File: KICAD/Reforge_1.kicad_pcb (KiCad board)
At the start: 2 copper layers, 61 x 77.8 mm, 92 parts, among them J1 USB_C_Receptacle_USB2.0_16P, J10 Conn_01x14_Pin, J11 Conn_01x12_Pin, J12 Conn_01x12_Pin, J14 Conn_01x12_Pin, J15 Conn_01x12_Pin, J3 Conn_01x02, J8 Conn_01x12_Pin, J9 Conn_01x14_Pin, Q1 SS8050, Q2 SS8050, SW1 SW_Push, SW2 SW_Push, U11 SN74LVC2G125DCUR, U2 CP2102N-Axx-xQFN28, U3 ICE40UP5K-SG48ITR, U4 AP2112K-1.2, U5 ESP32-WROOM-32D, U6 AMS1117-3.3, U8 W25Q32JVSS, Y1 SG-210STF

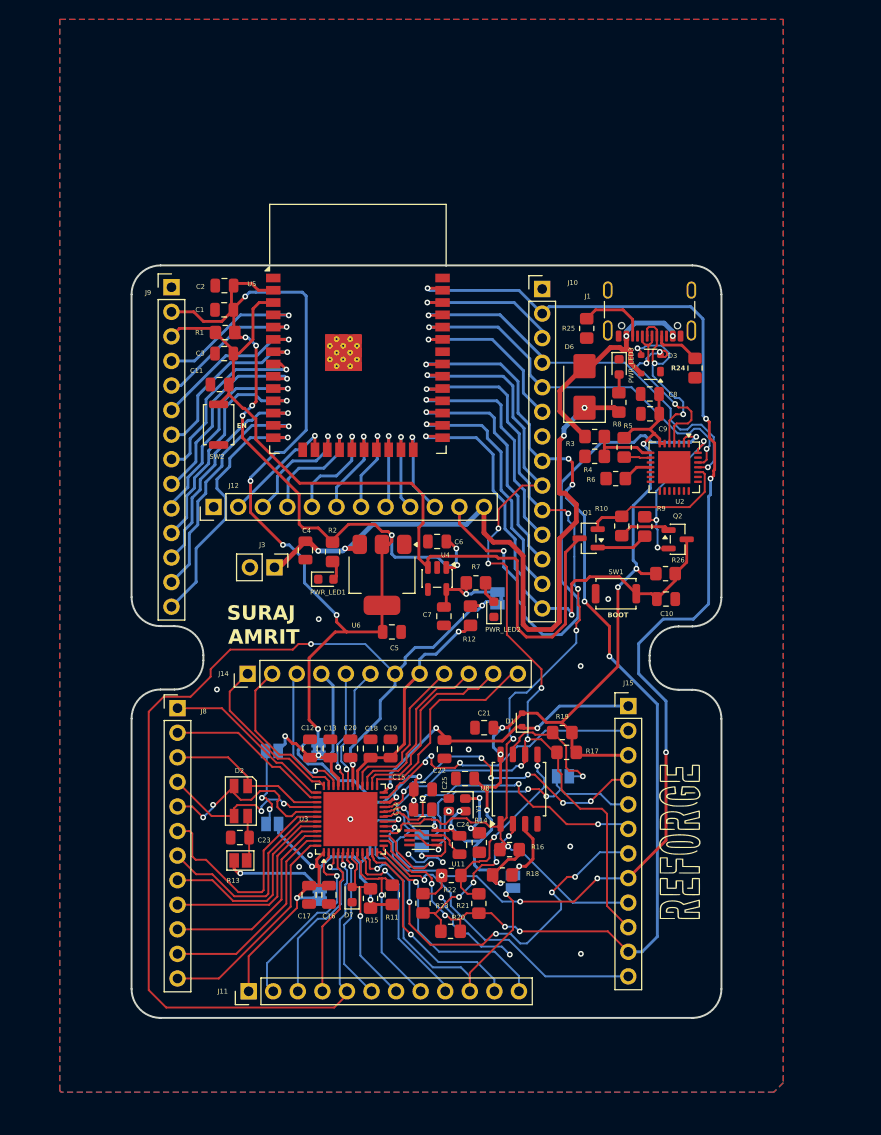
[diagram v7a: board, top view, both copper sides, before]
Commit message: Updated Schematic, Added mounting hole and some updates in PCB
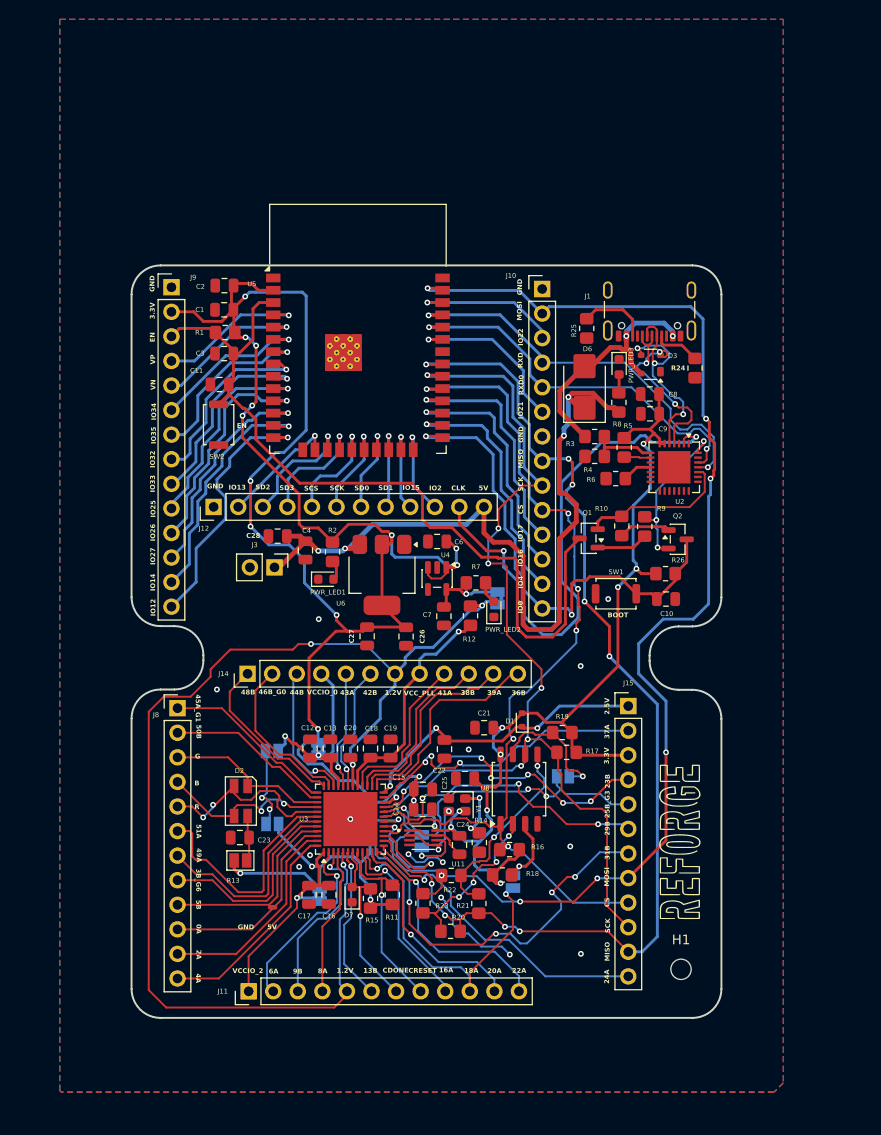
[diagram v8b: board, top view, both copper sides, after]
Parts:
- removed C5: 10uF, Capacitor_SMD:C_0805_2012Metric
- added C26: 22uF, Capacitor_SMD:C_0805_2012Metric, F.Cu at (136.7, 85.5)
- added C27: 0.1uF, Capacitor_SMD:C_0805_2012Metric, F.Cu at (132.7, 85.5)
- added C28: 0.1uF, Capacitor_SMD:C_0805_2012Metric, F.Cu at (123.4, 75.1)
- added H1: MountingHole, MountingHole:MountingHole_2.1mm, F.Cu at (165.1, 119.9)
- C4: value 22uF -> 10uF
- R10, R9: value 10R(5%) -> 10k(5%)
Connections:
- U4 pad 3: /EN -> /VDD33
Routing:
- net /VDD33: track 308.7 -> 316.5 mm
- net /EXT_5V: track 74.6 -> 81.7 mm
- net /EN: track 88.6 -> 84.2 mm
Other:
- board text added: "0A"
- board text added: "1.2V"
- board text added: "13B"
- board text added: "16A"
- board text added: "18A"
- board text added: "2.5V"
- board text added: "20A"
- board text added: "22A"
- board text added: "23B"
- board text added: "24A"
- board text added: "25B_G3"
- board text added: "29B"
- board text added: "2A"
- board text added: "3.3V"
- board text added: "31B"
- board text added: "36B"
- board text added: "37A"
- board text added: "38B"
- board text added: "39A"
- board text added: "3B_G6"
- board text added: "41A"
- board text added: "42B"
- board text added: "43A"
- board text added: "44B"
- board text added: "45A_G1"
- board text added: "46B_G0"
- board text added: "48B"
- board text added: "49A"
- board text added: "4A"
- board text added: "50B"
- board text added: "51A"
- board text added: "5B"
- board text added: "5V"
- board text added: "6A"
- board text added: "8A"
- board text added: "9B"
- board text added: "B"
- board text added: "CDONE"
- board text added: "CLK"
- board text added: "CRESET"
- board text added: "CS"
- board text added: "Designed by"
- board text added: "G"
- board text added: "GND"
- board text added: "IO0"
- board text added: "IO12"
- board text added: "IO13"
- board text added: "IO14"
- board text added: "IO15"
- board text added: "IO16"
- board text added: "IO17"
- board text added: "IO2"
- board text added: "IO21"
- board text added: "IO22"
- board text added: "IO25"
- board text added: "IO26"
- board text added: "IO27"
- board text added: "IO32"
- board text added: "IO33"
- board text added: "IO34"
- board text added: "IO35"
- board text added: "IO4"
- board text added: "MISO"
- board text added: "MOSI"
- board text added: "R"
- board text added: "RXD"
- board text added: "RXD0"
- board text added: "SCK"
- board text added: "SCS"
- board text added: "SD0"
- board text added: "SD1"
- board text added: "SD2"
- board text added: "SD3"
- board text added: "VCCIO_0"
- board text added: "VCCIO_2"
- board text added: "VCC_PLL"
- board text added: "VN"
- board text added: "VP"
